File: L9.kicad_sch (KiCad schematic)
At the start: 38 parts

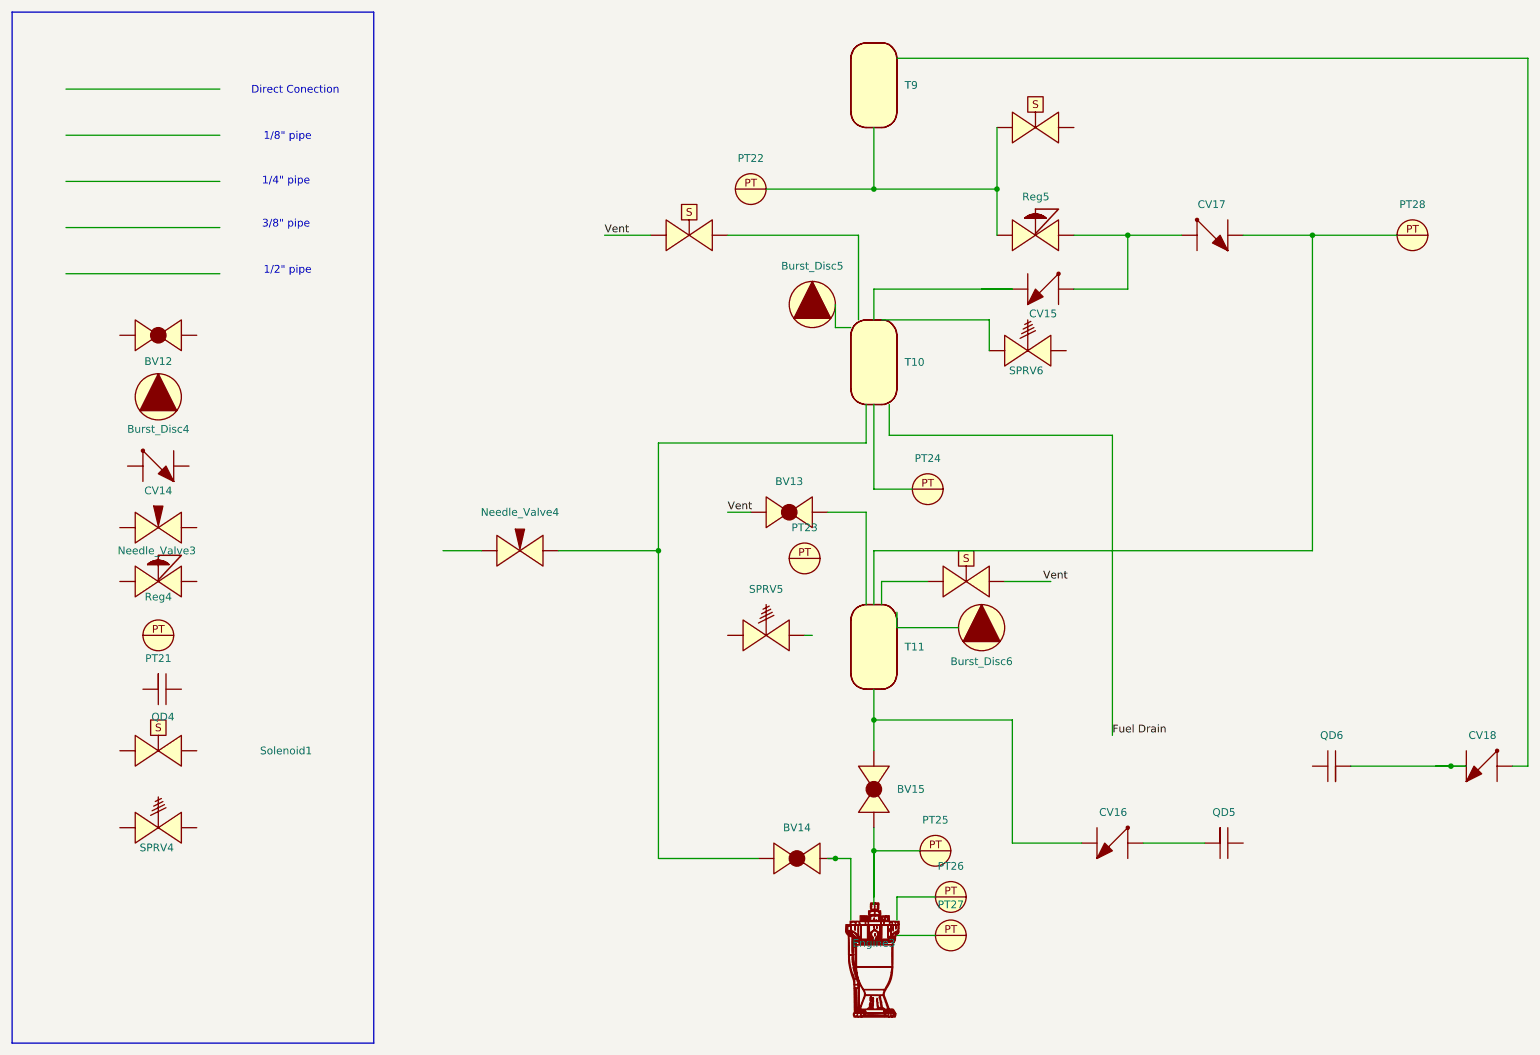
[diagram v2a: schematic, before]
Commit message: Updated igniter PID
+PT +nitrous pressure
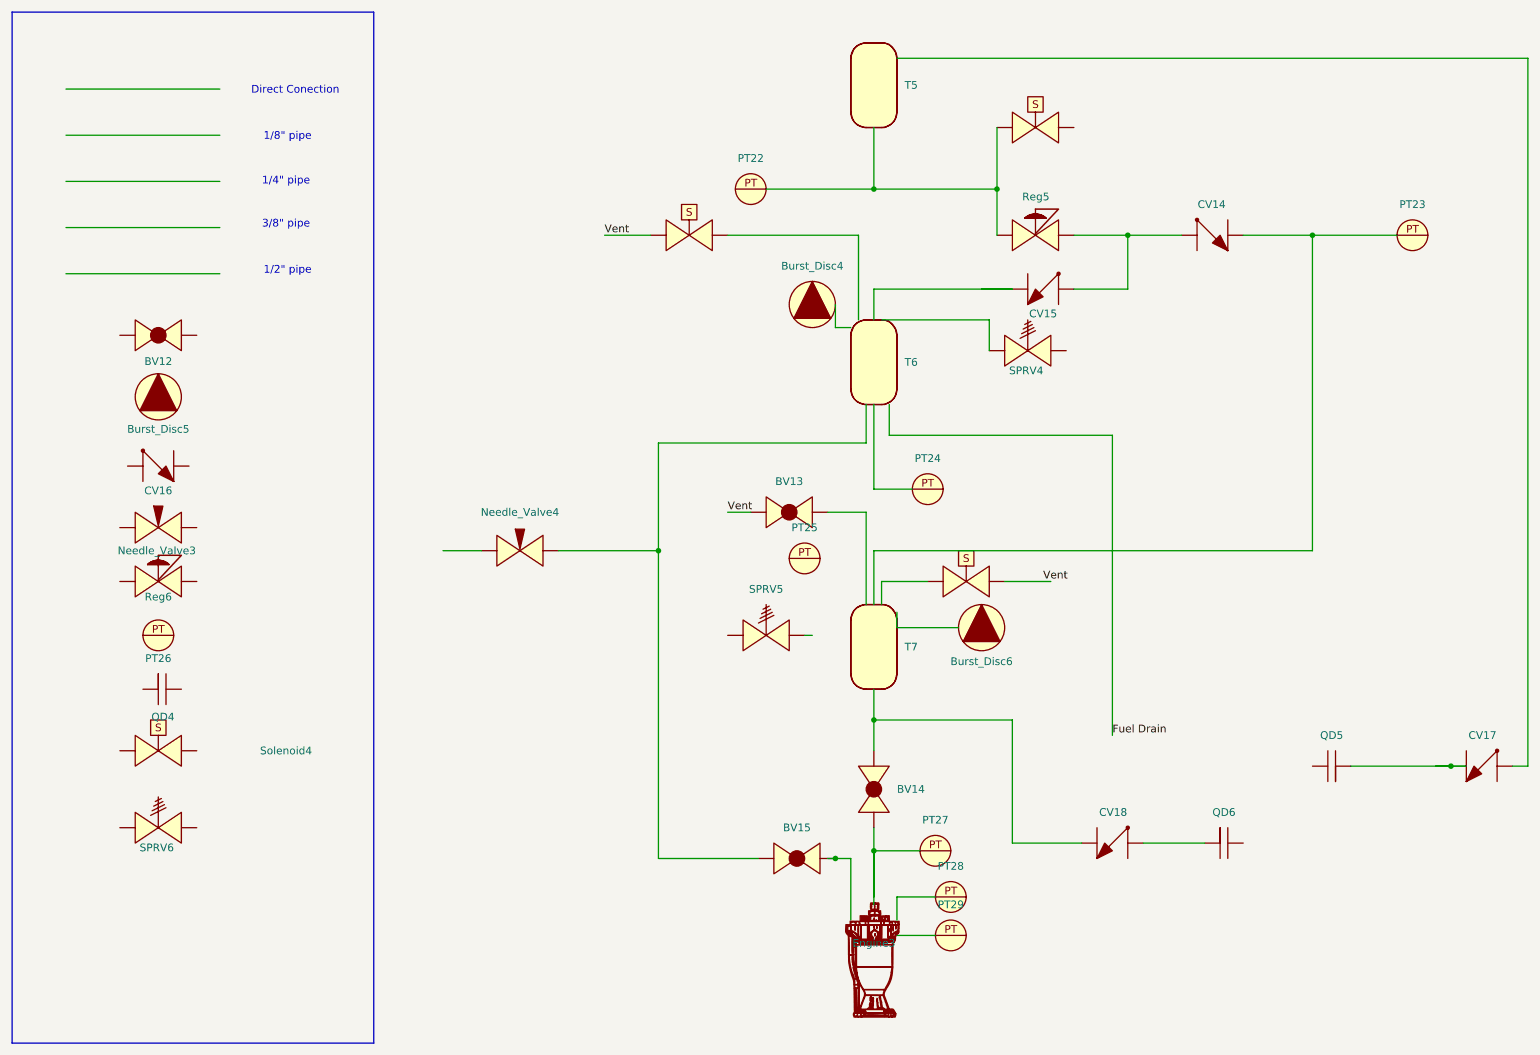
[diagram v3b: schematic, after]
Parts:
- renumbered BV15 to BV14, BV14 to BV15, Burst_Disc5 to Burst_Disc4, Burst_Disc4 to Burst_Disc5, CV17 to CV14, CV14 to CV16, CV18 to CV17, CV16 to CV18, PT28 to PT23, PT23 to PT25, PT21 to PT26, PT25 to PT27, PT26 to PT28, PT27 to PT29, QD6 to QD5, QD5 to QD6, Reg4 to Reg6, SPRV6 to SPRV4, SPRV4 to SPRV6, Solenoid4 to Solenoid1, Solenoid1 to Solenoid4, T9 to T5, T10 to T6, T11 to T7
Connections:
- net at QD6.: now also CV18.
- net at CV18.: now also BV14., T7.; no longer QD6.
- net at PT23.: now also CV14., T7.
- net at CV17.: now also QD5.
- net at QD5.: no longer CV17.
- net at Engine3.: now also BV14., PT27.; no longer BV15.
- net at PT28.: no longer Engine3.
- net at Needle_Valve4.: now also BV15.
- new net: CV14., CV15., Reg5.
- new net: PT22., Reg5., Solenoid1., T5.
- new net: BV15., Engine3.
- new net: Engine3., PT28.
- now unconnected: PT22., PT27., Solenoid1., T5.
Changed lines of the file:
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@@
 	(label "Vent"
 		(at 132.08 99.06 0)
-		(fields_autoplaced yes)
 		(effects
 			(font
@@
 	(label "Fuel Drain"
 		(at 195.58 135.89 0)
-		(fields_autoplaced yes)
 		(effects
 			(font
@@
 	(label "Vent"
 		(at 111.76 53.34 0)
-		(fields_autoplaced yes)
 		(effects
 			(font
@@
 	(label "Vent"
 		(at 184.15 110.49 0)
-		(fields_autoplaced yes)
 		(effects
 			(font
@@
 		(dnp no)
 		(fields_autoplaced yes)
-		(property "Reference" "QD5"
+		(property "Reference" "QD6"
 			(at 213.995 148.59 0)
 			(effects
@@
 			(project ""
 				(path "/045f1f05-3134-4b6d-91b6-463031104f1e/80d334bb-222a-483c-b02d-befc9811806d"
-					(reference "QD5")
+					(reference "QD6")
 					(unit 1)
 				)
@@
 		(dnp no)
 		(fields_autoplaced yes)
-		(property "Reference" "PT28"
+		(property "Reference" "PT23"
 			(at 245.11 48.26 0)
 			(effects
@@
 			(project ""
 				(path "/045f1f05-3134-4b6d-91b6-463031104f1e/80d334bb-222a-483c-b02d-befc9811806d"
-					(reference "PT28")
+					(reference "PT23")
 					(unit 1)
 				)
@@
 		(on_board yes)
 		(dnp no)
-		(property "Reference" "PT21"
+		(property "Reference" "PT26"
 			(at 38.1 123.19 0)
 			(effects
@@
 			(project ""
 				(path "/045f1f05-3134-4b6d-91b6-463031104f1e/80d334bb-222a-483c-b02d-befc9811806d"
-					(reference "PT21")
+					(reference "PT26")
 					(unit 1)
 				)
@@
 		(dnp no)
 		(fields_autoplaced yes)
-		(property "Reference" "CV18"
+		(property "Reference" "CV17"
 			(at 256.667 135.89 0)
 			(effects
@@
 			(project ""
 				(path "/045f1f05-3134-4b6d-91b6-463031104f1e/80d334bb-222a-483c-b02d-befc9811806d"
-					(reference "CV18")
+					(reference "CV17")
 					(unit 1)
 				)
@@
 		(dnp no)
 		(fields_autoplaced yes)
-		(property "Reference" "CV16"
+		(property "Reference" "CV18"
 			(at 195.707 148.59 0)
 			(effects
@@
 			(project ""
 				(path "/045f1f05-3134-4b6d-91b6-463031104f1e/80d334bb-222a-483c-b02d-befc9811806d"
-					(reference "CV16")
+					(reference "CV18")
 					(unit 1)
 				)
@@
 		(dnp no)
 		(fields_autoplaced yes)
-		(property "Reference" "T9"
+		(property "Reference" "T5"
 			(at 161.29 28.5749 0)
 			(effects
@@
 			(project ""
 				(path "/045f1f05-3134-4b6d-91b6-463031104f1e/80d334bb-222a-483c-b02d-befc9811806d"
-					(reference "T9")
+					(reference "T5")
 					(unit 1)
 				)
@@
 		(dnp no)
 		(fields_autoplaced yes)
-		(property "Reference" "CV17"
+		(property "Reference" "CV14"
 			(at 211.963 48.26 0)
 			(effects
@@
 			(project ""
 				(path "/045f1f05-3134-4b6d-91b6-463031104f1e/80d334bb-222a-483c-b02d-befc9811806d"
-					(reference "CV17")
+					(reference "CV14")
 					(unit 1)
 				)
@@
 		(dnp no)
 		(fields_autoplaced yes)
-		(property "Reference" "PT23"
+		(property "Reference" "PT25"
 			(at 144.78 101.6 0)
 			(effects
@@
 			(project ""
 				(path "/045f1f05-3134-4b6d-91b6-463031104f1e/80d334bb-222a-483c-b02d-befc9811806d"
-					(reference "PT23")
+					(reference "PT25")
 					(unit 1)
 				)
@@
 		(dnp no)
 		(fields_autoplaced yes)
-		(property "Reference" "PT27"
+		(property "Reference" "PT29"
 			(at 168.91 163.83 0)
 			(effects
@@
 			(project ""
 				(path "/045f1f05-3134-4b6d-91b6-463031104f1e/80d334bb-222a-483c-b02d-befc9811806d"
-					(reference "PT27")
+					(reference "PT29")
 					(unit 1)
 				)
@@
 		(on_board yes)
 		(dnp no)
-		(property "Reference" "CV14"
+		(property "Reference" "CV16"
 			(at 38.1 95.504 0)
 			(effects
@@
 			(project ""
 				(path "/045f1f05-3134-4b6d-91b6-463031104f1e/80d334bb-222a-483c-b02d-befc9811806d"
-					(reference "CV14")
+					(reference "CV16")
 					(unit 1)
 				)
@@
 		(dnp no)
 		(fields_autoplaced yes)
-		(property "Reference" "Burst_Disc5"
+		(property "Reference" "Burst_Disc4"
 			(at 146.05 58.42 0)
 			(effects
@@
 			(project ""
 				(path "/045f1f05-3134-4b6d-91b6-463031104f1e/80d334bb-222a-483c-b02d-befc9811806d"
-					(reference "Burst_Disc5")
+					(reference "Burst_Disc4")
 					(unit 1)
 				)
@@
 		(dnp no)
 		(fields_autoplaced yes)
-		(property "Reference" "BV14"
+		(property "Reference" "BV15"
 			(at 143.51 151.13 0)
 			(effects
@@
 			(project ""
 				(path "/045f1f05-3134-4b6d-91b6-463031104f1e/80d334bb-222a-483c-b02d-befc9811806d"
-					(reference "BV14")
+					(reference "BV15")
 					(unit 1)
 				)
@@
 		(on_board yes)
 		(dnp no)
-		(property "Reference" "Solenoid1"
+		(property "Reference" "Solenoid4"
 			(at 59.182 138.43 0)
 			(effects
@@
 			(project ""
 				(path "/045f1f05-3134-4b6d-91b6-463031104f1e/80d334bb-222a-483c-b02d-befc9811806d"
-					(reference "Solenoid1")
+					(reference "Solenoid4")
 					(unit 1)
 				)
@@
 		(on_board yes)
 		(dnp no)
-		(property "Reference" "SPRV6"
+		(property "Reference" "SPRV4"
 			(at 181.356 75.692 0)
 			(effects
@@
 			(project ""
 				(path "/045f1f05-3134-4b6d-91b6-463031104f1e/80d334bb-222a-483c-b02d-befc9811806d"
-					(reference "SPRV6")
+					(reference "SPRV4")
 					(unit 1)
 				)
@@
 		(dnp no)
 		(fields_autoplaced yes)
-		(property "Reference" "T11"
+		(property "Reference" "T7"
 			(at 161.29 121.2849 0)
 			(effects
@@
 			(project "P_IDs"
 				(path "/045f1f05-3134-4b6d-91b6-463031104f1e/80d334bb-222a-483c-b02d-befc9811806d"
-					(reference "T11")
+					(reference "T7")
 					(unit 1)
 				)
@@
 		(dnp no)
 		(fields_autoplaced yes)
-		(property "Reference" "T10"
+		(property "Reference" "T6"
 			(at 161.29 74.2949 0)
 			(effects
@@
 			(project "P_IDs"
 				(path "/045f1f05-3134-4b6d-91b6-463031104f1e/80d334bb-222a-483c-b02d-befc9811806d"
-					(reference "T10")
+					(reference "T6")
 					(unit 1)
 				)
@@
 		(dnp no)
 		(fields_autoplaced yes)
-		(property "Reference" "QD6"
+		(property "Reference" "QD5"
 			(at 231.775 135.89 0)
 			(effects
@@
 			(project ""
 				(path "/045f1f05-3134-4b6d-91b6-463031104f1e/80d334bb-222a-483c-b02d-befc9811806d"
-					(reference "QD6")
+					(reference "QD5")
 					(unit 1)
 				)
@@
 		(dnp no)
 		(fields_autoplaced yes)
-		(property "Reference" "PT26"
+		(property "Reference" "PT28"
 			(at 168.91 157.48 0)
 			(effects
@@
 			(project ""
 				(path "/045f1f05-3134-4b6d-91b6-463031104f1e/80d334bb-222a-483c-b02d-befc9811806d"
-					(reference "PT26")
+					(reference "PT28")
 					(unit 1)
 				)
@@
 		(on_board yes)
 		(dnp no)
-		(property "Reference" "Burst_Disc4"
+		(property "Reference" "Burst_Disc5"
 			(at 38.1 85.344 0)
 			(effects
@@
 			(project ""
 				(path "/045f1f05-3134-4b6d-91b6-463031104f1e/80d334bb-222a-483c-b02d-befc9811806d"
-					(reference "Burst_Disc4")
+					(reference "Burst_Disc5")
 					(unit 1)
 				)
@@
 		(on_board yes)
 		(dnp no)
-		(property "Reference" "SPRV4"
+		(property "Reference" "SPRV6"
 			(at 37.846 154.432 0)
 			(effects
@@
 			(project ""
 				(path "/045f1f05-3134-4b6d-91b6-463031104f1e/80d334bb-222a-483c-b02d-befc9811806d"
-					(reference "SPRV4")
+					(reference "SPRV6")
 					(unit 1)
 				)
@@
 		(dnp no)
 		(fields_autoplaced yes)
-		(property "Reference" "BV15"
+		(property "Reference" "BV14"
 			(at 160.02 144.7799 90)
 			(effects
@@
 			(project ""
 				(path "/045f1f05-3134-4b6d-91b6-463031104f1e/80d334bb-222a-483c-b02d-befc9811806d"
-					(reference "BV15")
+					(reference "BV14")
 					(unit 1)
 				)
@@
 		(dnp no)
 		(fields_autoplaced yes)
-		(property "Reference" "Solenoid4"
+		(property "Reference" "Solenoid1"
 			(at 182.88 26.67 0)
 			(effects
@@
 			(project ""
 				(path "/045f1f05-3134-4b6d-91b6-463031104f1e/80d334bb-222a-483c-b02d-befc9811806d"
-					(reference "Solenoid4")
+					(reference "Solenoid1")
 					(unit 1)
 				)
@@
 		(dnp no)
 		(fields_autoplaced yes)
-		(property "Reference" "PT25"
+		(property "Reference" "PT27"
 			(at 166.37 149.86 0)
 			(effects
@@
 			(project ""
 				(path "/045f1f05-3134-4b6d-91b6-463031104f1e/80d334bb-222a-483c-b02d-befc9811806d"
-					(reference "PT25")
+					(reference "PT27")
 					(unit 1)
 				)
@@
 		(on_board yes)
 		(dnp no)
-		(property "Reference" "Reg4"
+		(property "Reference" "Reg6"
 			(at 38.1 113.03 0)
 			(effects
@@
 			(project ""
 				(path "/045f1f05-3134-4b6d-91b6-463031104f1e/80d334bb-222a-483c-b02d-befc9811806d"
-					(reference "Reg4")
-					(unit 1)
-				)
+					(reference "Reg6")
+					(unit 1)
+				)

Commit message: replaced servo with solenoid
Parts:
- renumbered BV12 to BV11, BV13 to BV12, BV14 to BV13, BV15 to BV14
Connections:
- net at QD6.: now also CV18.
- net at CV18.: now also BV13., T7.; no longer QD6.
- net at PT23.: now also CV14., T7.
- net at CV17.: now also QD5.
- net at QD5.: no longer CV17.
- net at Engine3.: now also BV13., PT27.; no longer BV14.
- net at PT28.: no longer Engine3.
- net at Needle_Valve4.: now also BV14.
- new net: CV14., CV15., Reg5.
- new net: PT22., Reg5., Solenoid1., T5.
- new net: BV14., Engine3.
- new net: Engine3., PT28.
- now unconnected: PT22., PT27., Solenoid1., T5.
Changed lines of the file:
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@@
 		(dnp no)
 		(fields_autoplaced yes)
-		(property "Reference" "BV13"
+		(property "Reference" "BV12"
 			(at 142.24 93.98 0)
 			(effects
@@
 			(project ""
 				(path "/045f1f05-3134-4b6d-91b6-463031104f1e/80d334bb-222a-483c-b02d-befc9811806d"
-					(reference "BV13")
+					(reference "BV12")
 					(unit 1)
 				)
@@
 		(on_board yes)
 		(dnp no)
-		(property "Reference" "BV12"
+		(property "Reference" "BV11"
 			(at 38.1 74.168 0)
 			(effects
@@
 			(project ""
 				(path "/045f1f05-3134-4b6d-91b6-463031104f1e/80d334bb-222a-483c-b02d-befc9811806d"
-					(reference "BV12")
+					(reference "BV11")
 					(unit 1)
 				)
@@
 		(dnp no)
 		(fields_autoplaced yes)
-		(property "Reference" "BV15"
+		(property "Reference" "BV14"
 			(at 143.51 151.13 0)
 			(effects
@@
 			(project ""
 				(path "/045f1f05-3134-4b6d-91b6-463031104f1e/80d334bb-222a-483c-b02d-befc9811806d"
-					(reference "BV15")
+					(reference "BV14")
 					(unit 1)
 				)
@@
 		(dnp no)
 		(fields_autoplaced yes)
-		(property "Reference" "BV14"
+		(property "Reference" "BV13"
 			(at 160.02 144.7799 90)
 			(effects
@@
 			(project ""
 				(path "/045f1f05-3134-4b6d-91b6-463031104f1e/80d334bb-222a-483c-b02d-befc9811806d"
-					(reference "BV14")
-					(unit 1)
-				)
+					(reference "BV13")
+					(unit 1)
+				)

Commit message: rebase
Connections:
- net at QD6.: now also CV18.
- net at CV18.: now also BV13., T7.; no longer QD6.
- net at PT23.: now also CV14., T7.
- net at CV17.: now also QD5.
- net at QD5.: no longer CV17.
- net at Engine3.: now also BV13., PT27.; no longer BV14.
- net at PT28.: no longer Engine3.
- net at Needle_Valve4.: now also BV14.
- new net: CV14., CV15., Reg5.
- new net: PT22., Reg5., Solenoid1., T5.
- new net: BV14., Engine3.
- new net: Engine3., PT28.
- now unconnected: PT22., PT27., Solenoid1., T5.
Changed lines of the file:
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@@
 	(label "Vent"
 		(at 132.08 99.06 0)
+		(fields_autoplaced yes)
 		(effects
 			(font
@@
 	(label "Fuel Drain"
 		(at 195.58 135.89 0)
+		(fields_autoplaced yes)
 		(effects
 			(font
@@
 	(label "Vent"
 		(at 111.76 53.34 0)
+		(fields_autoplaced yes)
 		(effects
 			(font
@@
 	(label "Vent"
 		(at 184.15 110.49 0)
+		(fields_autoplaced yes)
 		(effects
 			(font
